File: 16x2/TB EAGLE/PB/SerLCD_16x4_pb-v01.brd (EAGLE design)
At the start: 87.7 x 144.8 mm, 25 parts, among them J1 AVR_PROG, J3 SER_LCD16X2, U1 5V Flying Jalapeno, U2 74LVC4066_MUX_1:1_X4

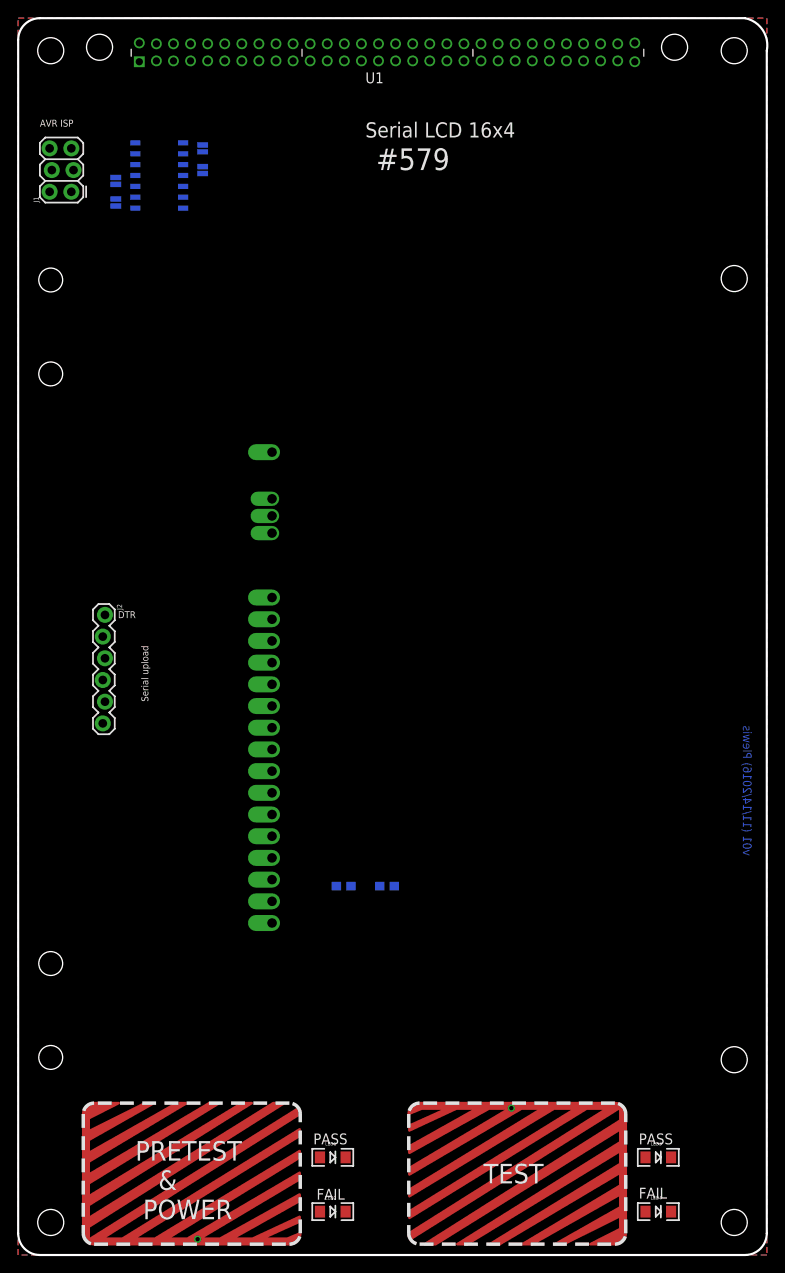
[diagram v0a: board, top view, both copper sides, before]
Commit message: finished up 16x4 (PB/PM/PF/WT)
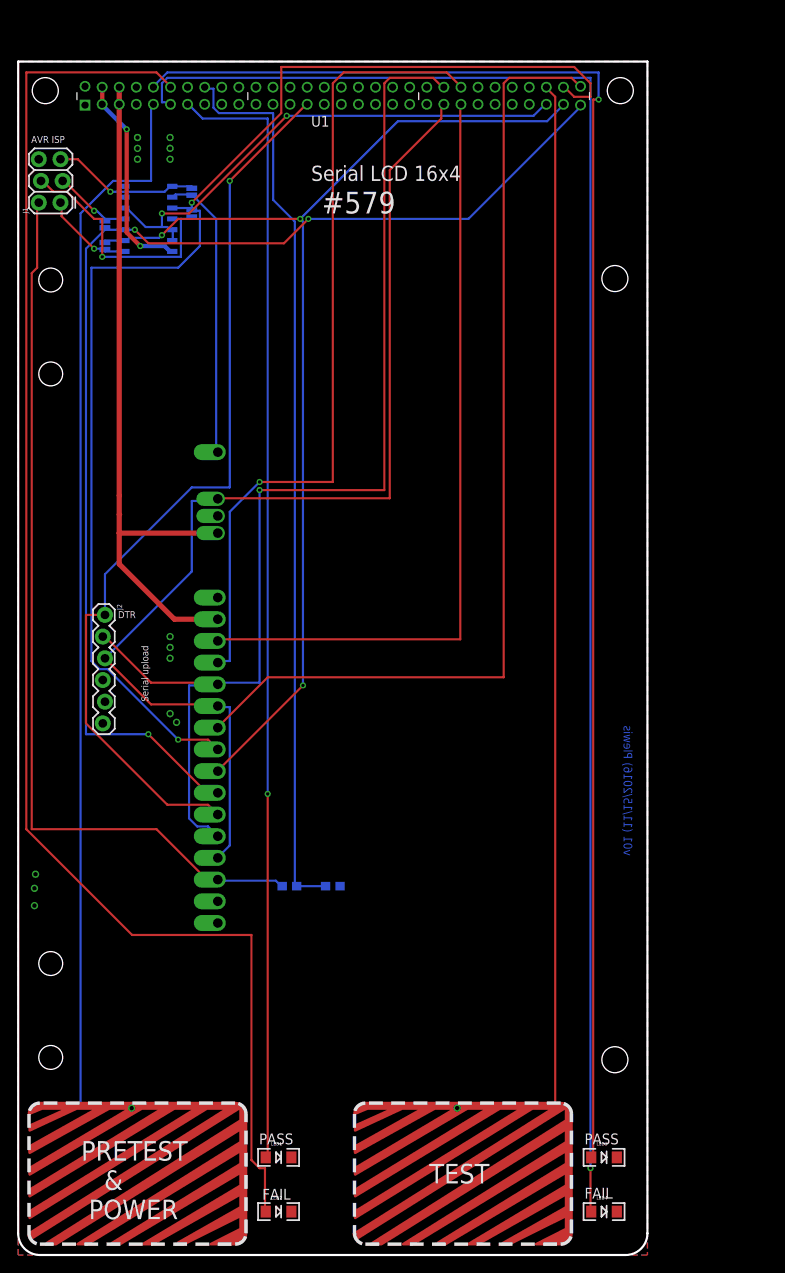
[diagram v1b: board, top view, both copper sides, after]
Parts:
- removed U$2, U$4, U$5, U$9: (no value), SparkFun:STAND-OFF-TIGHT
- moved U$3 14.0 mm to (69.8, 114.3)
- moved U$8 14.0 mm to (69.8, 22.9)
- moved U1 8.13 mm to (36.8, 139.7)
- moved 1 6.48 mm to (14.0, 10.2), turned to 0 degrees
- moved LED3 6.35 mm to (68.6, 11.4)
- moved LED4 6.35 mm to (68.6, 5.08)
- moved 2 6.35 mm to (52.1, 10.2)
- moved J3 6.35 mm to (57.1, 29.2)
- moved R1 6.35 mm to (31.8, 43.2)
- moved R2 6.35 mm to (36.8, 43.2)
- moved LED1 6.35 mm to (30.5, 11.4)
- moved LED2 6.35 mm to (30.5, 5.08)
- moved JP1 5.24 mm to (10.2, 118.1)
- moved JP2 5.24 mm to (10.2, 120.7)
- moved JP3 5.24 mm to (20.3, 124.5)
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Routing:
- net N$6: track 0.00 -> 186.6 mm, vias 0 -> 1
- net N$5: track 0.00 -> 180.7 mm, vias 0 -> 1
- net N$4: track 0.00 -> 171.2 mm
- net MOSI: track 0.00 -> 149.6 mm, vias 0 -> 2
- net SCK: track 0.00 -> 141.6 mm, vias 0 -> 3
- net RX1_FJ: track 0.00 -> 136.4 mm, vias 0 -> 1
- net N$3: track 0.00 -> 131.9 mm, vias 0 -> 1
- net N$2: track 0.00 -> 131.4 mm
- net TX1_FJ: track 0.00 -> 130.0 mm
- net N$1: track 0.00 -> 129.6 mm
- net MISO: track 0.00 -> 129.4 mm, vias 0 -> 3
- net CS: track 0.00 -> 115.1 mm
- net DTR_FJ: track 0.00 -> 107.0 mm, vias 0 -> 1
- net 3.3_VCC: track 0.00 -> 105.9 mm
- net N$7: track 0.00 -> 105.7 mm
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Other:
- board size 87.7 x 144.8 mm -> 73.7 x 139.7 mm
- board text added: "v01 (11/15/2016) Plewis"
- board text removed: "v01 (11/14/2016) Plewis"
